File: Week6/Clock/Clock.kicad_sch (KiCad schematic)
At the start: 48 parts, among them J1 Power_inlet_vertical, J2 Conn_01x06, SW2 Omron_B3F_SPST, U2 ATmega328-PU, U3 L7805_TO92, U4 DS1307_DIP-8, U5 MAX7219, U6 MAX7219, Y1 Crystal 16MHZ, Y2 Crystal_32768Hz

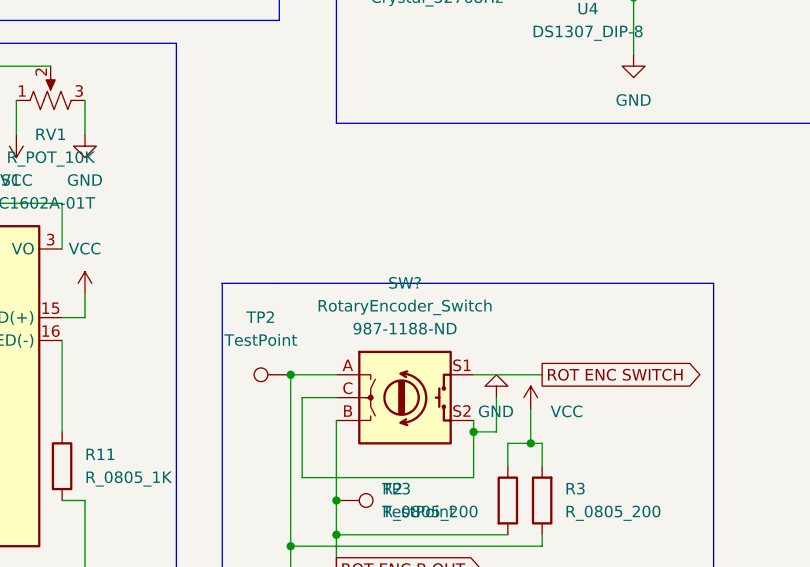
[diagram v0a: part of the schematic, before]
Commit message: Rot Encoder Update
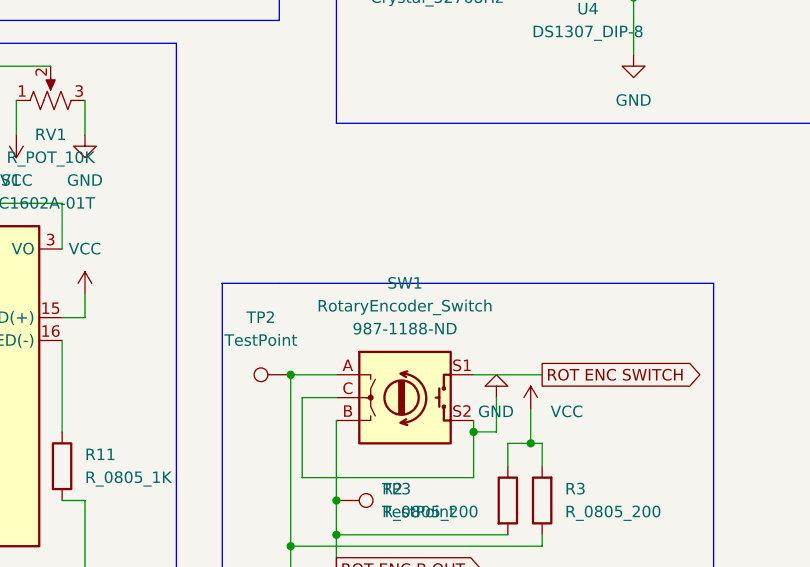
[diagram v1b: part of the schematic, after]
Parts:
- gave numbers to parts that had none: 1
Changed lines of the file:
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@@
   (symbol (lib_name "RotaryEncoder_Switch_1") (lib_id "HPS:RotaryEncoder_Switch") (at 92.71 95.25 0) (unit 1)
     (in_bom yes) (on_board yes) (fields_autoplaced)
-    (property "Reference" "SW?" (id 0) (at 92.71 82.55 0))
+    (property "Reference" "SW1" (id 0) (at 92.71 82.55 0))
     (property "Value" "RotaryEncoder_Switch" (id 1) (at 92.71 85.09 0))
     (property "Footprint" "footprints:RotaryEncoder_TT_EN11-Switch_Vertical_H20mm_CircularMountingHoles" (id 2) (at 88.9 91.186 0)
@@
       (reference "RV1") (unit 1) (value "R_POT_10K") (footprint "footprints:Potentiometer_Bourns_3386P_Vertical")
     )
+    (path "/d1f5403b-bbbd-4164-ba08-dace560dc8dc"
+      (reference "SW1") (unit 1) (value "RotaryEncoder_Switch") (footprint "footprints:RotaryEncoder_TT_EN11-Switch_Vertical_H20mm_CircularMountingHoles")
+    )
     (path "/b0579336-c97b-45cc-a8d9-5b76c366032d"
       (reference "SW2") (unit 1) (value "Omron_B3F_SPST") (footprint "footprints:SW_SPST_Omron_B3FS-100xP")
     )
-    (path "/d1f5403b-bbbd-4164-ba08-dace560dc8dc"
-      (reference "SW?") (unit 1) (value "RotaryEncoder_Switch") (footprint "footprints:RotaryEncoder_TT_EN11-Switch_Vertical_H20mm_CircularMountingHoles")
-    )
     (path "/5be55864-1840-4ba0-9935-063223afd7aa"

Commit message: Week 7 Update !
It's great :smile:
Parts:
- added C12: C_0805_1uf, footprints:C_0805_2012Metric, symbol HPS:C_0805_1uf
- added DO_TP1, RX_TP1, TP_GND1, TX_TP1: TestPoint, footprints:TestPoint_THTPad_D2.0mm_Drill1.0mm, symbol HPS:TestPoint
- renumbered TP2 to A_TP1, TP3 to B_TP1, TP4 to VBAT_TP1, TP1 to VCC_TP1
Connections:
- net GND: now also C12.1, TP_GND1.1
- net ROT ENC SWITCH: now also C12.2
- net RXD: now also RX_TP1.1
- net TXD: now also TX_TP1.1
- net at U5.24 (DOUT): now also DO_TP1.1

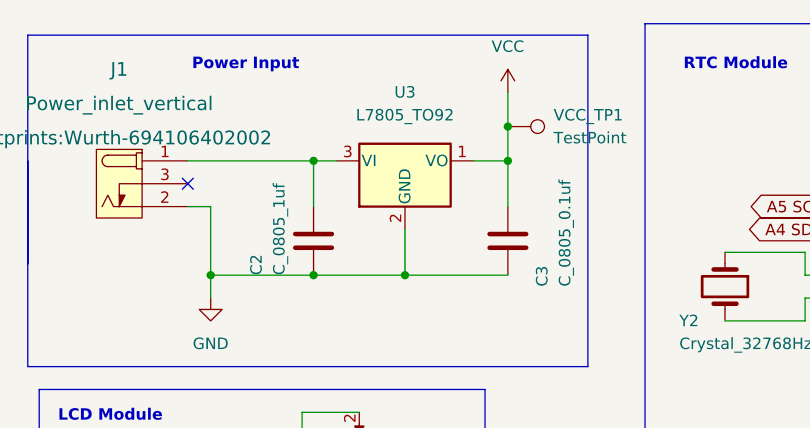
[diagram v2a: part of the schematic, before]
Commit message: Fixed PCB & Gerber
No more backsided SMT
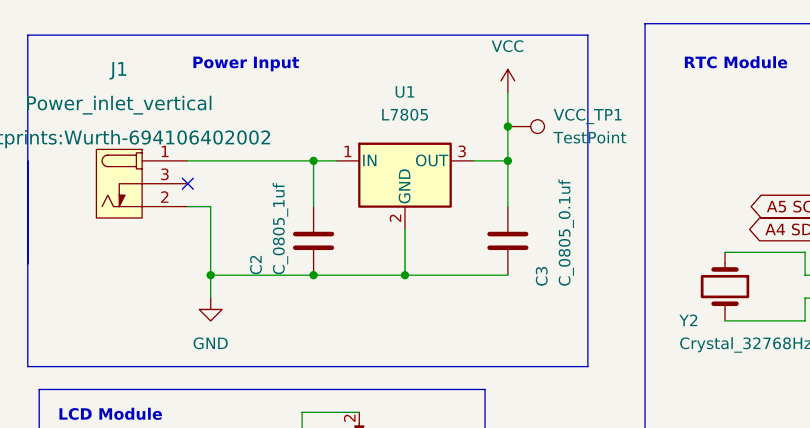
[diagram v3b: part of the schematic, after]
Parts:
- removed U3: L7805_TO92, footprints:TO-92_Inline, symbol HPS:L7805_TO92
- added U1: L7805, footprints:TO-252-2, symbol HPS:L7805
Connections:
- net GND: now also U1.2 (GND)
- net VCC: now also U1.3 (OUT)
- net at C2.1, J1.1 (POLE): now also U1.1 (IN)
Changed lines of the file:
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@@
     (pin "1")
+  )
+  (symbol (lib_id "HPS:L7805") (at 58.42 30.48 0) (unit 1)
+    (in_bom yes) (on_board yes) (fields_autoplaced)
+    (property "Reference" "U1" (id 0) (at 58.42 22.86 0))
+    (property "Value" "L7805" (id 1) (at 58.42 25.4 0))
+    (property "Footprint" "footprints:TO-252-2" (id 2) (at 59.055 34.29 0)
+      (effects (font (size 1.27 1.27) italic) (justify left) hide)
+    )
+    (property "Datasheet" "http://www.st.com/content/ccc/resource/technical/document/datasheet/41/4f/b3/b0/12/d4/47/88/CD00000444.pdf/files/CD00000444.pdf/jcr:content/translations/en.CD00000444.pdf" (id 3) (at 58.42 31.75 0)
+      (effects (font (size 1.27 1.27)) hide)
+    )
+    (property "Digikey PN" "497-7255-1-ND" (id 4) (at 58.42 30.48 0)
+      (effects (font (size 1.27 1.27)) hide)
+    )
+    (property "MPN" "L7805CDT-TR" (id 5) (at 58.42 30.48 0)
+      (effects (font (size 1.27 1.27)) hide)
+    )
+    (property "MFG" "STMicroelectronics" (id 6) (at 58.42 30.48 0)
+      (effects (font (size 1.27 1.27)) hide)
+    )
+    (pin "1")
+    (pin "2")
+    (pin "3")
   )
   (symbol (lib_id "HPS:R_0805_10K") (at 165.1 139.7 180) (unit 1)
@@
     (pin "1")
     (pin "2")
-  )
-  (symbol (lib_id "HPS:L7805_TO92") (at 58.42 30.48 0) (unit 1)
-    (in_bom yes) (on_board yes) (fields_autoplaced)
-    (property "Reference" "U3" (id 0) (at 58.42 22.86 0))
-    (property "Value" "L7805_TO92" (id 1) (at 58.42 25.4 0))
-    (property "Footprint" "footprints:TO-92_Inline" (id 2) (at 58.42 53.34 0)
-      (effects (font (size 1.27 1.27) italic) hide)
-    )
-    (property "Datasheet" "http://www.st.com/content/ccc/resource/technical/document/datasheet/15/55/e5/aa/23/5b/43/fd/CD00000446.pdf/files/CD00000446.pdf/jcr:content/translations/en.CD00000446.pdf" (id 3) (at 58.42 31.75 0)
-      (effects (font (size 1.27 1.27)) hide)
-    )
-    (property "MFG" "STMicroelectronics" (id 4) (at 58.42 48.26 0)
-      (effects (font (size 1.27 1.27)) hide)
-    )
-    (property "MPN" "L7805CV" (id 5) (at 58.42 50.8 0)
-      (effects (font (size 1.27 1.27)) hide)
-    )
-    (property "Digikey PN" "497-1443-5-ND" (id 6) (at 58.42 55.88 0)
-      (effects (font (size 1.27 1.27)) hide)
-    )
-    (property "Mouser PN" "N/A" (id 7) (at 58.42 58.42 0)
-      (effects (font (size 1.27 1.27)) hide)
-    )
-    (pin "1")
-    (pin "2")
-    (pin "3")
   )
   (symbol (lib_id "HPS:R_0805_1K") (at 54.61 102.87 0) (unit 1)
@@
       (reference "TX_TP1") (unit 1) (value "TestPoint") (footprint "footprints:TestPoint_THTPad_D2.0mm_Drill1.0mm")
     )
+    (path "/2630566b-5f52-4125-8967-91a2fcd86ef3"
+      (reference "U1") (unit 1) (value "L7805") (footprint "footprints:TO-252-2")
+    )
     (path "/d1c2159c-cf17-43fd-99c0-c5e908f82a85"
       (reference "U2") (unit 1) (value "ATmega328-PU") (footprint "footprints:DIP-28_W7.62mm")
     )
-    (path "/713dc497-2007-402d-95c6-6840496e22c5"
-      (reference "U3") (unit 1) (value "L7805_TO92") (footprint "footprints:TO-92_Inline")
-    )
     (path "/d392e20e-5454-4c20-afd4-d6bb399d3b51"

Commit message: Uploaded Student Designs :)
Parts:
- removed C1: 10uf, footprints:C_0805_2012Metric, symbol HPS:C_0805_10uf
- removed C7, C8: C_0805_1uf, footprints:C_0805_2012Metric, symbol HPS:C_0805_1uf
- removed R10, R2, R3: R_0805_200, footprints:R_0805_2012Metric, symbol HPS:R_0805_1K
- removed R12, R13: R_0805_2.2K, footprints:R_0805_2012Metric, symbol HPS:R_0805_2.2K
- removed R9: R_0805_4.7K, footprints:R_0805_2012Metric, symbol HPS:R_0805_4.7K
- added C1, C13: C_0805_0.1uf, footprints:C_0805_2012Metric, symbol HPS:C_0805_0.1uf
- added C7, C8: C_0805_10uf, footprints:C_0805_2012Metric, symbol HPS:C_0805_10uf
- added D3: LED_0805, footprints:LED_0805_2012Metric, symbol HPS:LED_0805
- added R10, R2, R3, R9: R_0805_10K, footprints:R_0805_2012Metric, symbol HPS:R_0805_10K
- added R12, R13: R_0805_4.7K, footprints:R_0805_2012Metric, symbol HPS:R_0805_4.7K
- added R14: R_0805_1K, footprints:R_0805_2012Metric, symbol HPS:R_0805_1K
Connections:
- net A4 SDA: now also R13.2
- net A5 SCK: now also R12.2
- net GND: now also C1.2, C13.2, C7.2, C8.2, D3.1 (K), R10.2
- net ROT ENC A OUT: now also R3.2
- net ROT ENC B OUT: now also R2.2
- net ROT ENC SWITCH: now also R9.1
- net SCK: now also R14.1
- net VCC: now also C7.1, C8.1, R12.1, R13.1, R2.1, R3.1, R9.2
- net at U2.21 (AREF): now also C1.1, C13.1
- net at SW2.4 (B): now also R10.1
- net at R8.2: now also U6.18 (ISET)
- new net: D3.2 (A), R14.2
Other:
- note added: "Blinky LED"
- note added: "Ground Test Point"
- moved on the sheet: TP_GND1
